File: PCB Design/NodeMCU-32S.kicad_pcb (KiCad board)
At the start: 2 copper layers, 86.9 x 63.7 mm, 18 parts, among them J1 Screw_Terminal_01x02, J2 Screw_Terminal_01x02, J3 Screw_Terminal_01x04, J5 Screw_Terminal_01x03, Q1 IRFZ44N, SW1 SW_DPDT_x2, U1 ESP32-NodeMCU-32s, U2 Generic_5v_Module

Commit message: corrected PCB symbols
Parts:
- R3: value 220k -> 220Ω
- R4: value 330k -> 330Ω
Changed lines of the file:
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@@
       (effects (font (size 1 1) (thickness 0.15)))
     )
-    (fp_text value "330k" (at 4.9022 -0.0508 90) (layer "F.SilkS")
+    (fp_text value "330Ω" (at 4.9022 -0.0508 90) (layer "F.SilkS")
       (effects (font (size 1 1) (thickness 0.15)))
     )
@@
       (effects (font (size 1 1) (thickness 0.15)))
     )
-    (fp_text value "220k" (at 4.9022 0.0762 90) (layer "F.SilkS")
-      (effects (font (size 1 1) (thickness 0.15)))
-    )
+    (fp_text value "220Ω" (at 4.9022 0.0762 90) (layer "F.SilkS")
+      (effects (font (size 1 1) (thickness 0.15)))
+    )

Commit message: slight DC buck converter change
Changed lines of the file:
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@@
     )
     (fp_line (start -12.7 -10.16) (end 10.16 -10.16) (layer "F.SilkS") (width 0.12))
+    (fp_line (start -12.7 7.62) (end -12.7 -10.16) (layer "F.SilkS") (width 0.12))
     (fp_line (start 10.16 -10.16) (end 10.16 7.62) (layer "F.SilkS") (width 0.12))
-    (fp_line (start -12.7 7.62) (end -12.7 -10.16) (layer "F.SilkS") (width 0.12))
     (fp_line (start 10.16 7.62) (end -12.7 7.62) (layer "F.SilkS") (width 0.12))
-    (pad "1" thru_hole circle (at -10.16 -5.08) (size 1.524 1.524) (drill 0.762) (layers *.Cu *.Mask)
+    (pad "1" thru_hole circle (at -10.414 -7.62) (size 1.524 1.524) (drill 0.762) (layers *.Cu *.Mask)
       (net 2 "GND") (pinfunction "IN-") (pintype "input"))
-    (pad "1" thru_hole circle (at -10.16 -7.62) (size 1.524 1.524) (drill 0.762) (layers *.Cu *.Mask)
+    (pad "1" thru_hole circle (at -10.414 -5.08) (size 1.524 1.524) (drill 0.762) (layers *.Cu *.Mask)
       (net 2 "GND") (pinfunction "IN-") (pintype "input"))
-    (pad "2" thru_hole circle (at -10.16 2.54) (size 1.524 1.524) (drill 0.762) (layers *.Cu *.Mask)
+    (pad "2" thru_hole circle (at -10.414 5.08) (size 1.524 1.524) (drill 0.762) (layers *.Cu *.Mask)
       (net 1 "VCC") (pinfunction "IN+") (pintype "input"))
-    (pad "2" thru_hole circle (at -10.16 5.08) (size 1.524 1.524) (drill 0.762) (layers *.Cu *.Mask)
+    (pad "2" thru_hole circle (at -10.414 2.54) (size 1.524 1.524) (drill 0.762) (layers *.Cu *.Mask)
       (net 1 "VCC") (pinfunction "IN+") (pintype "input"))
-    (pad "3" thru_hole circle (at 7.874 -5.08) (size 1.524 1.524) (drill 0.762) (layers *.Cu *.Mask)
+    (pad "3" thru_hole circle (at 8.128 -5.08) (size 1.524 1.524) (drill 0.762) (layers *.Cu *.Mask)
       (net 2 "GND") (pinfunction "5v-") (pintype "output"))
-    (pad "3" thru_hole circle (at 7.874 -7.62) (size 1.524 1.524) (drill 0.762) (layers *.Cu *.Mask)
+    (pad "3" thru_hole circle (at 8.128 -7.62) (size 1.524 1.524) (drill 0.762) (layers *.Cu *.Mask)
       (net 2 "GND") (pinfunction "5v-") (pintype "output"))
-    (pad "4" thru_hole circle (at 7.874 2.54) (size 1.524 1.524) (drill 0.762) (layers *.Cu *.Mask)
+    (pad "4" thru_hole circle (at 8.128 2.54) (size 1.524 1.524) (drill 0.762) (layers *.Cu *.Mask)
       (net 5 "+5V") (pinfunction "5v") (pintype "output"))
-    (pad "4" thru_hole circle (at 7.874 5.08) (size 1.524 1.524) (drill 0.762) (layers *.Cu *.Mask)
+    (pad "4" thru_hole circle (at 8.128 5.08) (size 1.524 1.524) (drill 0.762) (layers *.Cu *.Mask)
       (net 5 "+5V") (pinfunction "5v") (pintype "output"))
   )
@@
   (segment (start 128.316 86.6445) (end 134.6251 86.6445) (width 0.25) (layer "F.Cu") (net 40))
   (via (at 104.784 82.8714) (size 0.8) (drill 0.4) (layers "F.Cu" "B.Cu") (net 40))
-  (segment (start 104.784 82.8714) (end 101.049 86.6065) (width 0.25) (layer "B.Cu") (net 40))
+  (segment (start 104.352 82.8714) (end 100.6169 86.6065) (width 0.25) (layer "B.Cu") (net 40))
   (segment (start 99.9236 86.6065) (end 99.9236 87.7316) (width 0.25) (layer "B.Cu") (net 40))
-  (segment (start 101.049 86.6065) (end 99.9236 86.6065) (width 0.25) (layer "B.Cu") (net 40))
+  (segment (start 100.6169 86.6065) (end 99.9236 86.6065) (width 0.25) (layer "B.Cu") (net 40))
+  (segment (start 104.784 82.8714) (end 104.352 82.8714) (width 0.25) (layer "B.Cu") (net 40))
 )

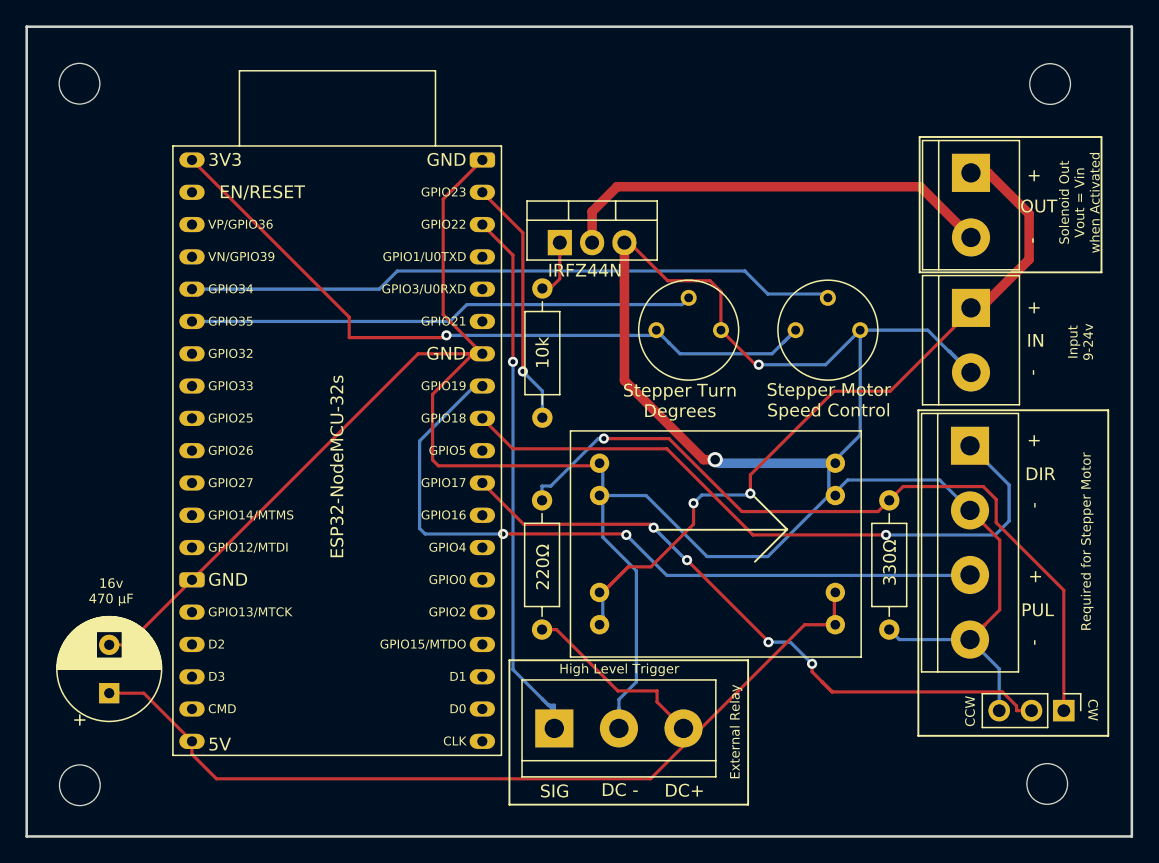
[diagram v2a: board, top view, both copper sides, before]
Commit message: drill hole changes
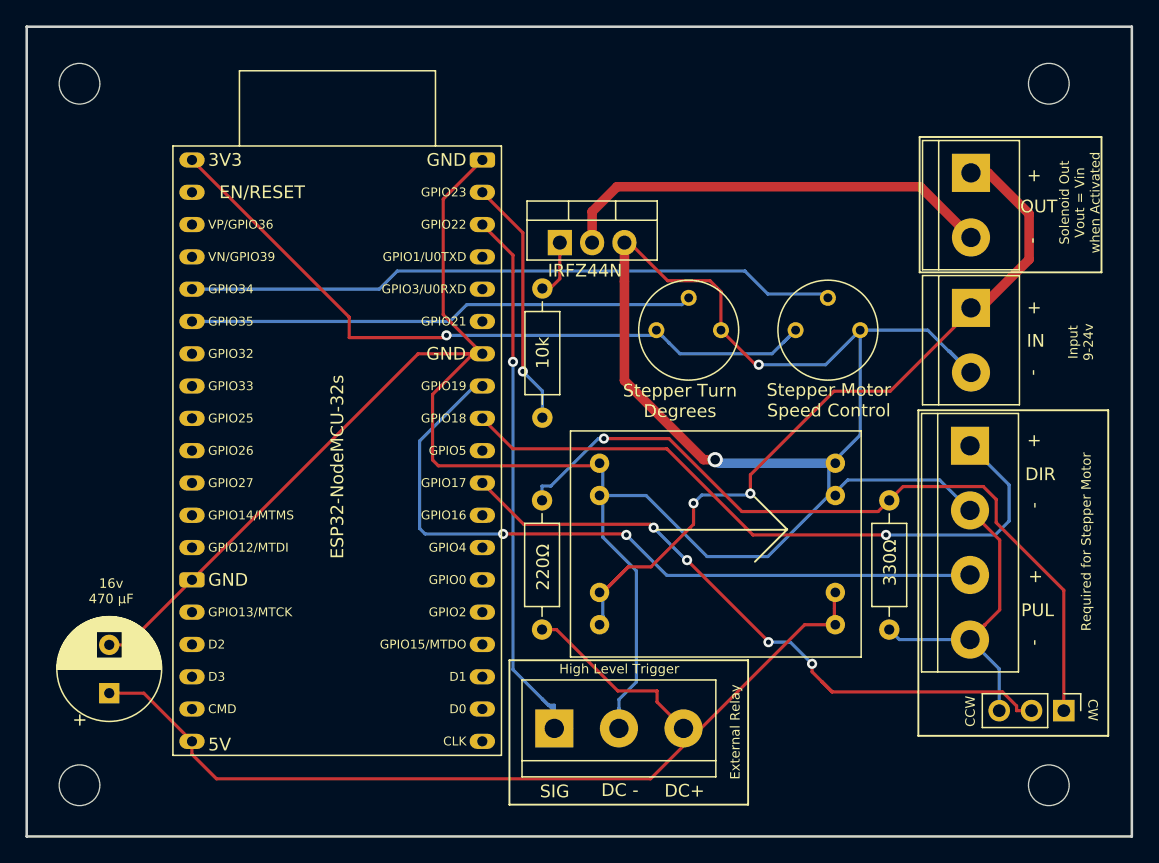
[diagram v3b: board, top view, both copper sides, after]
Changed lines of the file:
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@@
     (fp_circle (center 0 0) (end 3.2 0) (layer "Cmts.User") (width 0.15) (fill none))
     (fp_circle (center 0 0) (end 3.45 0) (layer "F.CrtYd") (width 0.05) (fill none))
-    (pad "" np_thru_hole circle (at 0 0) (size 3.2 3.2) (drill 3.2) (layers *.Cu *.Mask))
+    (pad "" np_thru_hole circle (at 0 0) (size 3.2 3.2) (drill 3.2) (layers F&B.Cu *.Mask))
   )
   (footprint "Resistor_THT:R_Axial_DIN0207_L6.3mm_D2.5mm_P10.16mm_Horizontal" (layer "F.Cu")
@@
     (fp_circle (center 0 0) (end 3.2 0) (layer "Cmts.User") (width 0.15) (fill none))
     (fp_circle (center 0 0) (end 3.45 0) (layer "F.CrtYd") (width 0.05) (fill none))
-    (pad "" np_thru_hole circle (at 0 0) (size 3.2 3.2) (drill 3.2) (layers *.Cu *.Mask))
+    (pad "" np_thru_hole circle (at 0.127 0.1016) (size 3.2 3.2) (drill 3.2) (layers F&B.Cu *.Mask))
   )
   (footprint "Potentiometer_THT:Potentiometer_Bourns_3339P_Vertical" (layer "F.Cu")
@@
     (fp_circle (center 0 0) (end 3.2 0) (layer "Cmts.User") (width 0.15) (fill none))
     (fp_circle (center 0 0) (end 3.45 0) (layer "F.CrtYd") (width 0.05) (fill none))
-    (pad "" np_thru_hole circle (at 0 0) (size 3.2 3.2) (drill 3.2) (layers *.Cu *.Mask))
+    (pad "" np_thru_hole circle (at -0.0254 0) (size 3.2 3.2) (drill 3.2) (layers F&B.Cu *.Mask))
   )
   (footprint "MountingHole:MountingHole_3.2mm_M3" (layer "F.Cu")
@@
     (fp_circle (center 0 0) (end 3.2 0) (layer "Cmts.User") (width 0.15) (fill none))
     (fp_circle (center 0 0) (end 3.45 0) (layer "F.CrtYd") (width 0.05) (fill none))
-    (pad "" np_thru_hole circle (at 0 0) (size 3.2 3.2) (drill 3.2) (layers *.Cu *.Mask))
+    (pad "" np_thru_hole circle (at -0.1016 -0.0254) (size 3.2 3.2) (drill 3.2) (layers F&B.Cu *.Mask))
   )
   (footprint "Connector_PinHeader_2.54mm:PinHeader_1x03_P2.54mm_Vertical" (layer "F.Cu")
